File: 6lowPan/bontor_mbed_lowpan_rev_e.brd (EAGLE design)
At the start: 98 x 107 mm, 170 parts, among them IC1 SIM900, IC2 74HC595D, IC3 74HC595D, IC4 ADE7758RW, IC5 74HC595D, J1 U.FL, U2 W5500, X1 NX2520SA

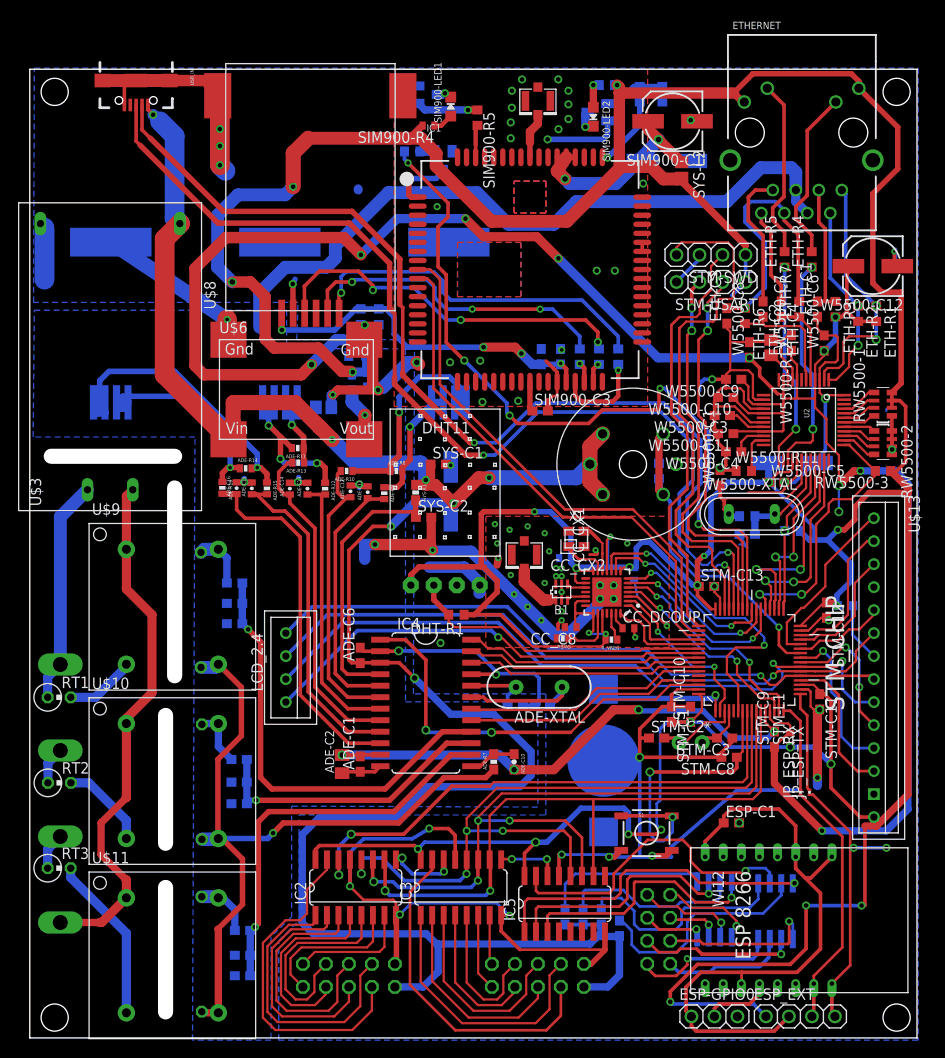
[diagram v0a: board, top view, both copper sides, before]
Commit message: update silkscreen and delete USB micro hole
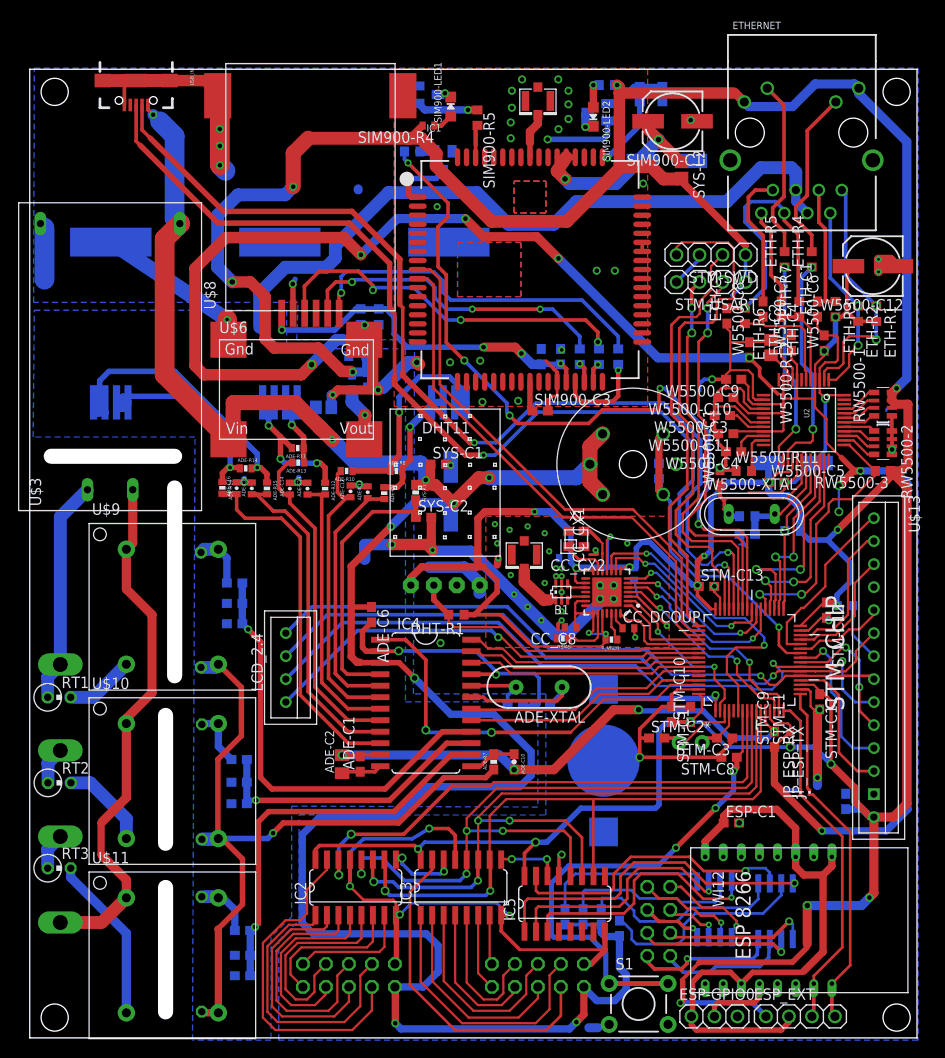
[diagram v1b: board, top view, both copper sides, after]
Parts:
- added LCD_C1: 100nF, rcl:C0603
- S1: device SparkFun-Electromechanical:TACTILE-SWITCH-SMD -> SparkFun-Electromechanical:TACTILE-PTH
- moved S1 18.9 mm to (67.2, 3.75)
- moved ADE-C6 4.67 mm to (37.8, 46.8), turned to 270 degrees
- moved JP1 0.88 mm to (69.5, 12.9)
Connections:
- net DGND: now also LCD_C1.2
- net VDD: now also LCD_C1.1
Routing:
- net DGND: track 425.6 -> 385.2 mm, vias 73 -> 72
- net SWD_NRST: track 33.8 -> 56.3 mm, vias 2 -> 3
- net +5V: track 258.3 -> 271.4 mm, vias 7 -> 9
- net VDD: track 578.7 -> 567.8 mm, vias 25 -> 24
- net ESP_TX: track 31.6 -> 27.6 mm, vias 2 -> 0
- net CH1_IN: track 34.9 -> 32.3 mm
- net N$5: track 24.7 -> 22.7 mm
- net CH2_B: track 17.9 -> 16.2 mm
- net N$6: track 26.7 -> 25.2 mm
- net T: track 5.34 -> 4.08 mm
- net CH2_IN: track 36.7 -> 37.4 mm
- net CH1_B: track 14.0 -> 14.6 mm
- net R: track 25.3 -> 24.7 mm
